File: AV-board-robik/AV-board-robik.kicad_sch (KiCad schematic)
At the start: 28 parts, among them J1 Mini-DIN-8, J2 Conn_01x09_Pin, J3 Conn_01x09, Q1 BC547, Q2 BC547, Q3 BC547, Q4 BC547, U2 74LS241

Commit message: finished board
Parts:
- removed J1: Mini-DIN-8, w_conn_av:minidin-8, symbol Connector:Mini-DIN-8
- removed J2: Conn_01x09_Pin, Connector_PinHeader_2.54mm:PinHeader_1x09_P2.54mm_Vertical, symbol Connector:Conn_01x09_Pin
- added J4: Conn_01x09, Connector_PinHeader_2.54mm:PinHeader_1x09_P2.54mm_Horizontal, symbol Connector_Generic:Conn_01x09
- J3: footprint (none) -> Connector_PinHeader_2.54mm:PinHeader_1x09_P2.54mm_Horizontal
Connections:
- net +12V: now also J4.8 (Pin_8)
- net +5V: now also J4.7 (Pin_7)
- net AUDIO: now also J4.2 (Pin_2)
- net B: now also J4.6 (Pin_6)
- net G: now also J4.5 (Pin_5)
- net GND: now also J3.6 (Pin_6), J4.9 (Pin_9)
- net R: now also J4.4 (Pin_4)
- net SYNC: now also J4.1 (Pin_1)
- net Y: now also J4.3 (Pin_3)
- net MD-2: now reaches D1.1 (K), R17.2
- net MD-2: now also J3.3 (Pin_3)
- net MD-8: now reaches R11.2
- net MD-8: now also J3.2 (Pin_2)
- net MD-5: now reaches RV1.2
- net MD-5: now also J3.1 (Pin_1)
- net MD-7: now reaches J3.4 (Pin_4)
- net MD-7: now also R13.2
- net MD-4: now reaches J3.7 (Pin_7)
- net MD-4: now also R14.2
- net MD-3: now reaches J3.8 (Pin_8)
- net MD-3: now also R16.2
- net MD-6: now reaches J3.9 (Pin_9)
- net MD-6: now also R15.2
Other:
- moved on the sheet: D1, J3, R16, R17

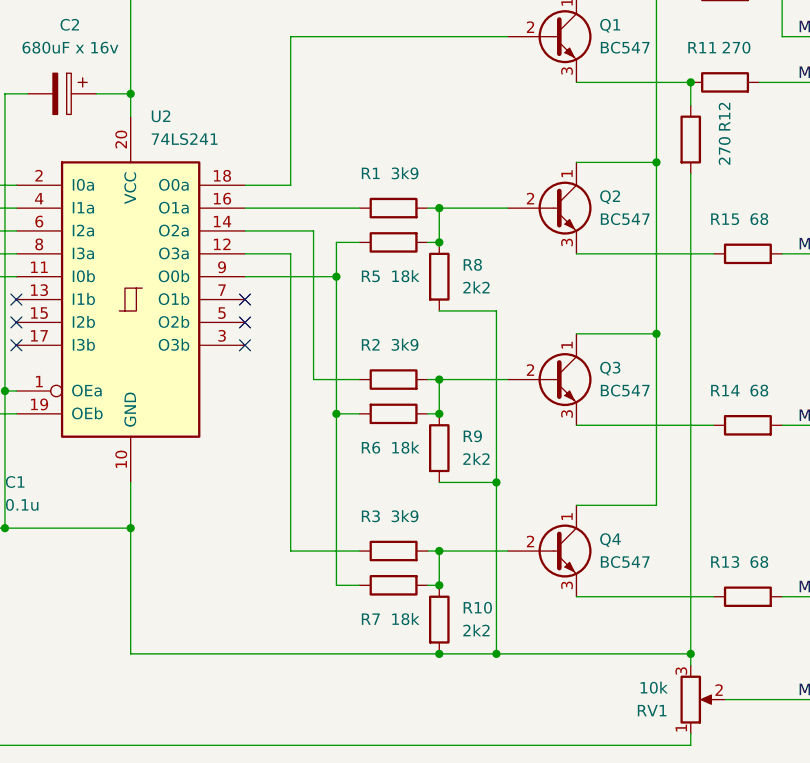
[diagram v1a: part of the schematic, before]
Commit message: Aligned resistors values for usage with 74LS logic that improves color brightness
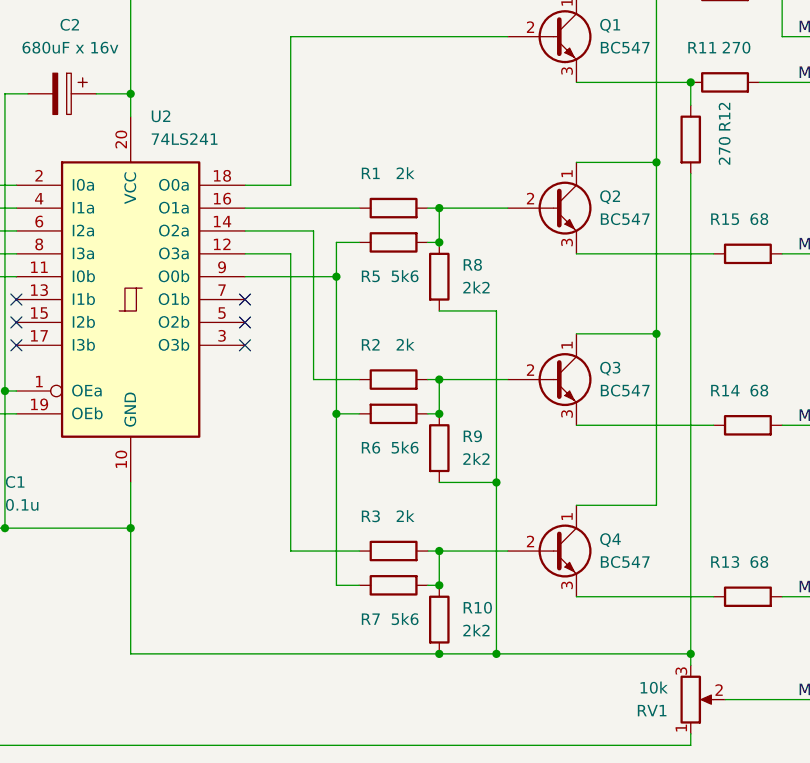
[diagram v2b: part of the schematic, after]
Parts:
- R1, R2, R3: value 3k9 -> 2k
- R5, R6, R7: value 18k -> 5k6
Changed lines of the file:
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@@
       (effects (font (size 1.27 1.27)))
     )
-    (property "Value" "3k9" (at 138.43 109.22 90)
+    (property "Value" "2k" (at 138.43 109.22 90)
       (effects (font (size 1.27 1.27)))
     )
@@
       (effects (font (size 1.27 1.27)))
     )
-    (property "Value" "18k" (at 138.43 82.55 90)
+    (property "Value" "5k6" (at 138.43 82.55 90)
       (effects (font (size 1.27 1.27)))
     )
@@
       (effects (font (size 1.27 1.27)))
     )
-    (property "Value" "18k" (at 138.43 120.65 90)
+    (property "Value" "5k6" (at 138.43 120.65 90)
       (effects (font (size 1.27 1.27)))
     )
@@
       (effects (font (size 1.27 1.27)))
     )
-    (property "Value" "3k9" (at 138.43 90.17 90)
+    (property "Value" "2k" (at 138.43 90.17 90)
       (effects (font (size 1.27 1.27)))
     )
@@
       (effects (font (size 1.27 1.27)))
     )
-    (property "Value" "18k" (at 138.43 101.6 90)
+    (property "Value" "5k6" (at 138.43 101.6 90)
       (effects (font (size 1.27 1.27)))
     )
@@
       (effects (font (size 1.27 1.27)))
     )
-    (property "Value" "3k9" (at 138.43 71.12 90)
-      (effects (font (size 1.27 1.27)))
-    )
+    (property "Value" "2k" (at 138.43 71.12 90)
+      (effects (font (size 1.27 1.27)))
+    )
